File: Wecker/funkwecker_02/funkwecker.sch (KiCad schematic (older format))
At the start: 20 parts, among them J1 DCF77-Connector, J2 Debug-Interface, J3 LED-Display Connector (TM1637), SW1 Hauptschalter, U1 MCP1702-3302, U2 STM8L051F3P, U8 MCP1702-5002, Y1 HC49U 16MHz

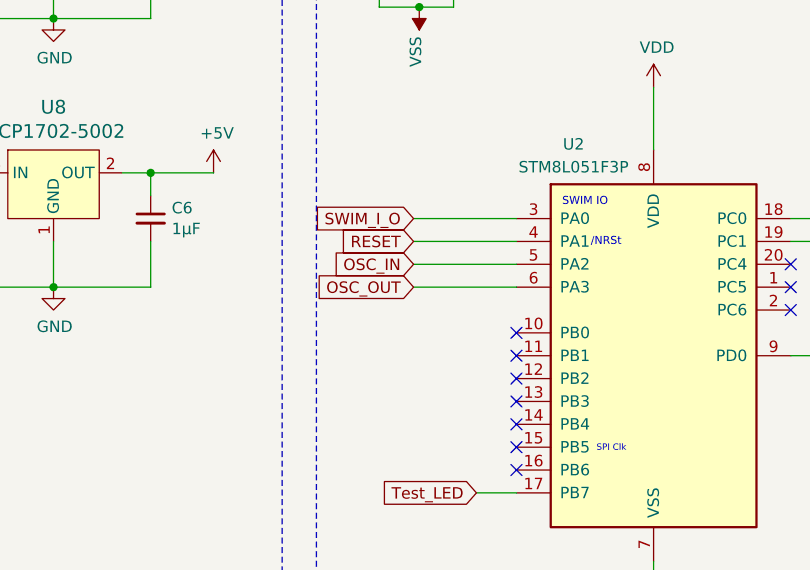
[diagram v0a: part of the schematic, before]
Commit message: 2.Revision angefangen
NRST Kondensator hinzugefügt
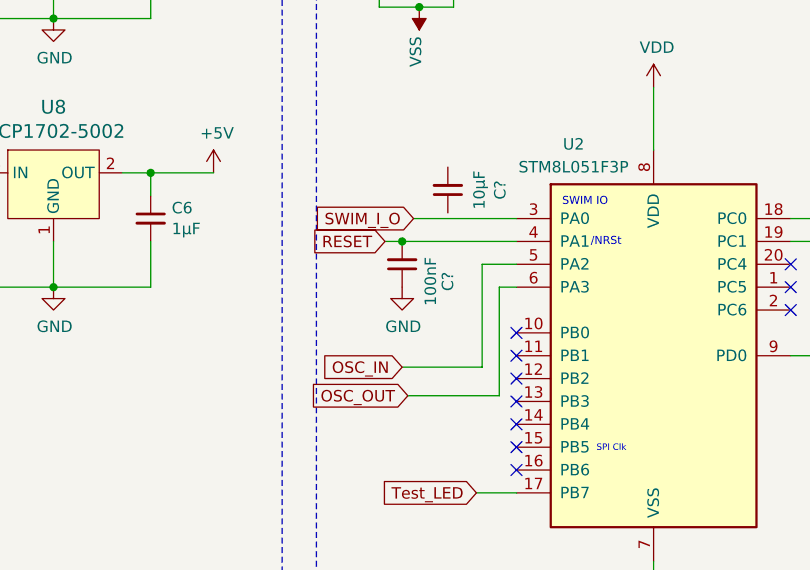
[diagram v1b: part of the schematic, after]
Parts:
- added C?: 10µF, Capacitor_THT:C_Disc_D7.0mm_W2.5mm_P5.00mm, symbol funkwecker-rescue:C_Small-Device
- added C?: 100nF, Capacitor_THT:C_Disc_D7.0mm_W2.5mm_P5.00mm, symbol funkwecker-rescue:C_Small-Device
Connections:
- net GND: now also C?.1
- net RESET: now also C?.2
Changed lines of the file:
@@
 Sheet 1 1
 Title "Funkwecker"
-Date "2021-12-12"
-Rev "0.1"
+Date "2021-12-21"
+Rev "0.2"
 Comp ""
 Comment1 ""
@@
 Text Notes 3075 800  0    50   ~ 0
 µC\n
-Text GLabel 3450 2675 0    50   Input ~ 0
+Text GLabel 3325 2675 0    50   Input ~ 0
 RESET
 Text GLabel 3450 2575 0    50   Input ~ 0
@@
 Text Notes 4250 3600 0    28   ~ 0
 SPI Clk\n
-Wire Wire Line
-	3900 2675 3450 2675
 Text GLabel 3725 3775 0    50   Input ~ 0
 Test_LED
 Wire Wire Line
 	3725 3775 3900 3775
-Text GLabel 3450 2875 0    50   Input ~ 0
+Text GLabel 3425 3350 0    50   Input ~ 0
 OSC_OUT
 $Comp
@@
 	1    0    0    -1
 $EndComp
-Text GLabel 3450 2775 0    50   Input ~ 0
+Text GLabel 3400 3225 0    50   Input ~ 0
 OSC_IN
-Wire Wire Line
-	3450 2775 3900 2775
-Wire Wire Line
-	3450 2875 3900 2875
 NoConn ~ 5100 2875
 NoConn ~ 5100 2975
@@
 	0    -1   -1   0
 $EndComp
+$Comp
+L funkwecker-rescue:C_Small-Device C?
+U 1 1 61C20B95
+P 3600 2450
+F 0 "C?" V 3371 2450 50  0000 C CNN
+F 1 "10µF" V 3462 2450 50  0000 C CNN
+F 2 "Capacitor_THT:C_Disc_D7.0mm_W2.5mm_P5.00mm" H 3600 2450 50  0001 C CNN
+F 3 "~" H 3600 2450 50  0001 C CNN
+	1    3600 2450
+	-1   0    0    1
+$EndComp
+$Comp
+L funkwecker-rescue:C_Small-Device C?
+U 1 1 61C265FF
+P 3400 2775
+F 0 "C?" V 3200 2850 50  0000 C CNN
+F 1 "100nF" V 3275 2850 50  0000 C CNN
+F 2 "Capacitor_THT:C_Disc_D7.0mm_W2.5mm_P5.00mm" H 3400 2775 50  0001 C CNN
+F 3 "~" H 3400 2775 50  0001 C CNN
+	1    3400 2775
+	-1   0    0    1
+$EndComp
+Wire Wire Line
+	3325 2675 3400 2675
+Connection ~ 3400 2675
+Wire Wire Line
+	3400 2675 3900 2675
+$Comp
+L funkwecker-rescue:GND-power #PWR?
+U 1 1 61C2841D
+P 3400 2875
+F 0 "#PWR?" H 3400 2625 50  0001 C CNN
+F 1 "GND" H 3405 2702 50  0000 C CNN
+F 2 "" H 3400 2875 50  0001 C CNN
+F 3 "" H 3400 2875 50  0001 C CNN
+	1    3400 2875
+	1    0    0    -1
+$EndComp
+Wire Wire Line
+	3900 2875 3825 2875
+Wire Wire Line
+	3825 2875 3825 3350
+Wire Wire Line
+	3825 3350 3425 3350
+Wire Wire Line
+	3900 2775 3750 2775
+Wire Wire Line
+	3750 2775 3750 3225
+Wire Wire Line
+	3750 3225 3400 3225
 $EndSCHEMATC

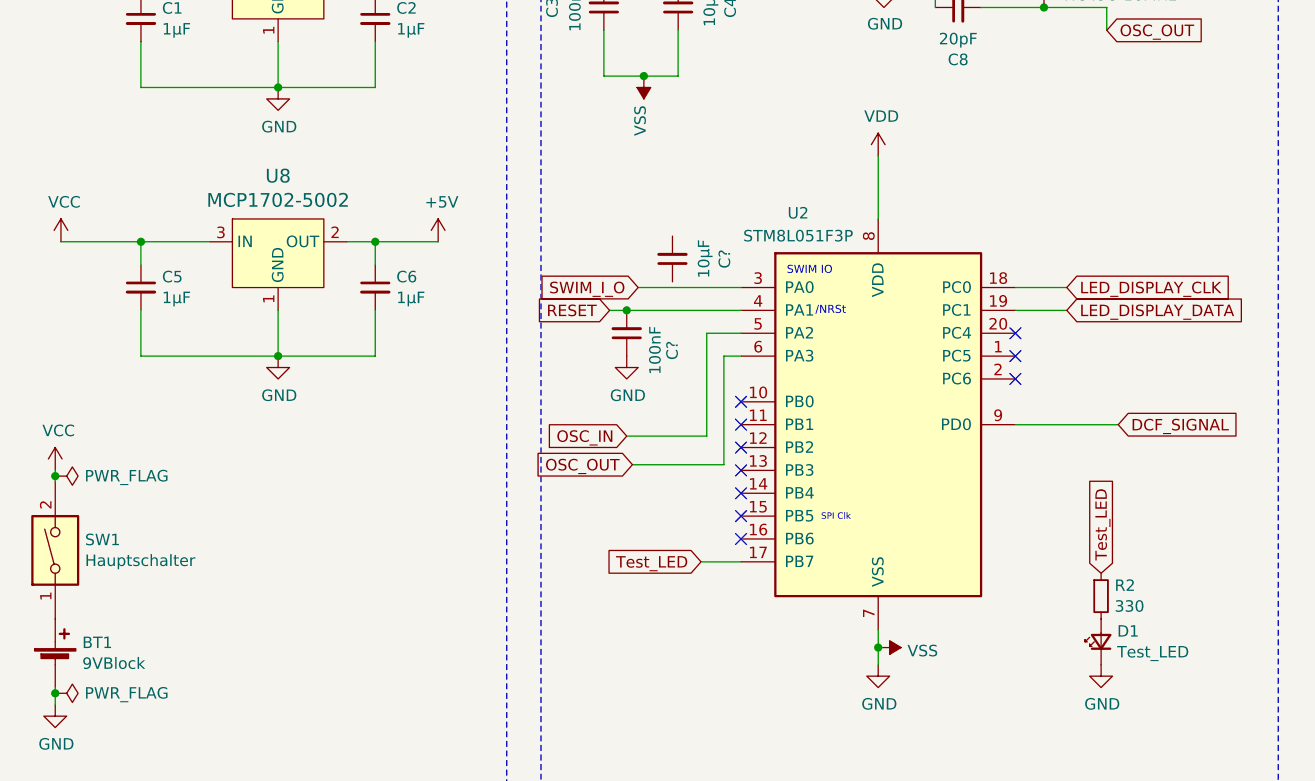
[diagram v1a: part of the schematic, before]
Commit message: Rev 2: Fehler korrigiert und neue Anordnung
Fehler:
-Fehlender Kondensator am RESET-Pin
-Fehlerhaftes Layout für beide Spannungsregler korrigiert
-Benötigten Platz verringert
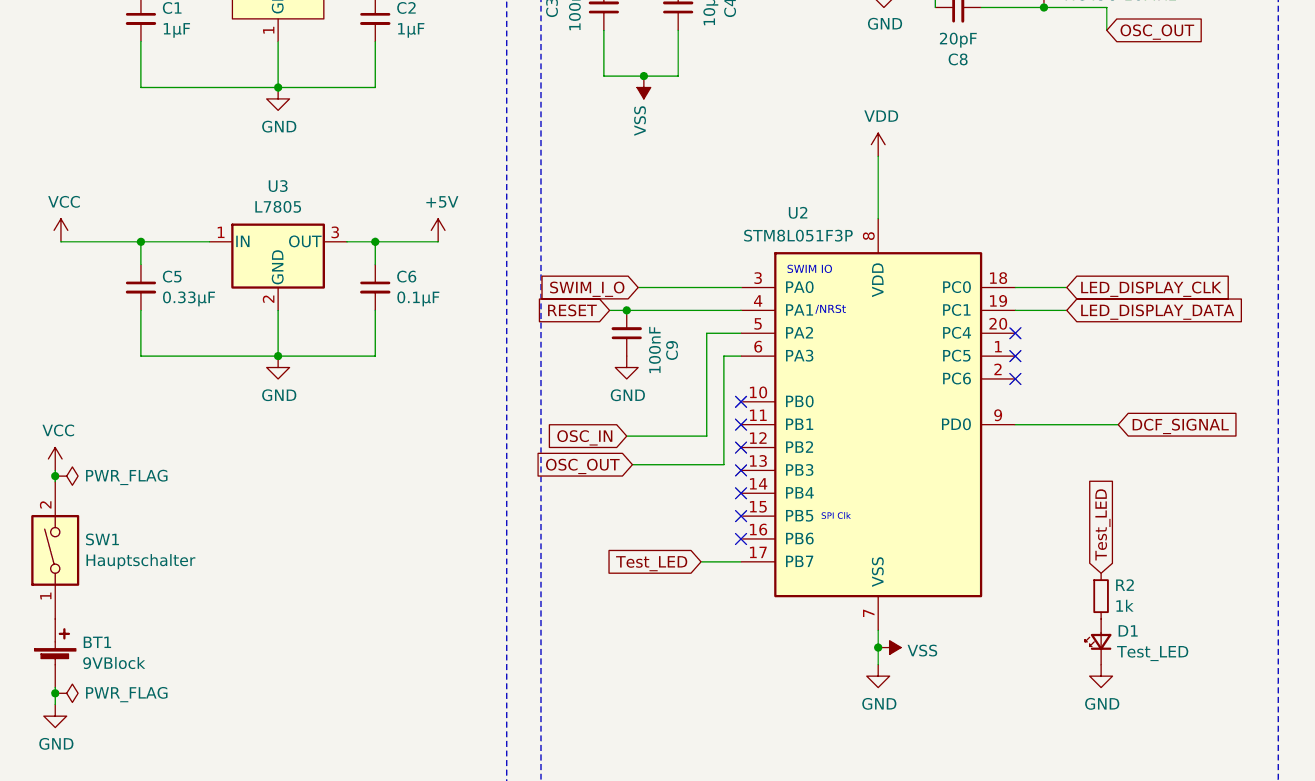
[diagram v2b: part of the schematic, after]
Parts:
- removed C?: 10µF, Capacitor_THT:C_Disc_D7.0mm_W2.5mm_P5.00mm, symbol funkwecker-rescue:C_Small-Device
- removed U8: MCP1702-5002, Package_TO_SOT_THT:TO-92, symbol funkwecker-rescue:MCP1700T-3302E_TT-dk_PMIC-Voltage-Regulators-Linear
- added U3: L7805, Package_TO_SOT_THT:TO-220-3_Vertical, symbol Regulator_Linear:L7805
- C1, C2: footprint Capacitor_THT:CP_Radial_D10.0mm_P2.50mm -> Capacitor_THT:C_Disc_D7.0mm_W2.5mm_P5.00mm
- C5: value 1µF -> 0.33µF; footprint Capacitor_THT:CP_Radial_D10.0mm_P2.50mm -> Capacitor_THT:C_Disc_D7.0mm_W2.5mm_P5.00mm
- C6: value 1µF -> 0.1µF; footprint Capacitor_THT:CP_Radial_D10.0mm_P2.50mm -> Capacitor_THT:C_Disc_D7.0mm_W2.5mm_P5.00mm
- R2: value 330 -> 1k
- gave numbers to parts that had none: 1
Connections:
- net +5V: now also U3.3 (OUT)
- net GND: now also U3.2 (GND)
- net VCC: now also U3.1 (IN)
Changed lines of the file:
@@
 F 0 "C1" H 1367 1446 50  0000 L CNN
 F 1 "1µF" H 1367 1355 50  0000 L CNN
-F 2 "Capacitor_THT:CP_Radial_D10.0mm_P2.50mm" H 1275 1400 50  0001 C CNN
+F 2 "Capacitor_THT:C_Disc_D7.0mm_W2.5mm_P5.00mm" H 1275 1400 50  0001 C CNN
 F 3 "~" H 1275 1400 50  0001 C CNN
 	1    1275 1400
@@
 F 0 "C2" H 2392 1446 50  0000 L CNN
 F 1 "1µF" H 2392 1355 50  0000 L CNN
-F 2 "Capacitor_THT:CP_Radial_D10.0mm_P2.50mm" H 2300 1400 50  0001 C CNN
+F 2 "Capacitor_THT:C_Disc_D7.0mm_W2.5mm_P5.00mm" H 2300 1400 50  0001 C CNN
 F 3 "~" H 2300 1400 50  0001 C CNN
 	1    2300 1400
@@
 	2300 1700 1875 1700
 $Comp
-L funkwecker-rescue:VCC-power #PWR0102
-U 1 1 61AA11C1
-P 925 1200
-F 0 "#PWR0102" H 925 1050 50  0001 C CNN
-F 1 "VCC" H 940 1373 50  0000 C CNN
-F 2 "" H 925 1200 50  0001 C CNN
-F 3 "" H 925 1200 50  0001 C CNN
-	1    925  1200
-	1    0    0    -1
-$EndComp
-$Comp
 L funkwecker-rescue:VCC-power #PWR0104
 U 1 1 61AA832C
@@
 F 3 "" H 900 3375 50  0001 C CNN
 	1    900  3375
-	1    0    0    -1
-$EndComp
-$Comp
-L funkwecker-rescue:VDD-power #PWR0105
-U 1 1 61AA994D
-P 2575 1200
-F 0 "#PWR0105" H 2575 1050 50  0001 C CNN
-F 1 "VDD" H 2590 1373 50  0000 C CNN
-F 2 "" H 2575 1200 50  0001 C CNN
-F 3 "" H 2575 1200 50  0001 C CNN
-	1    2575 1200
 	1    0    0    -1
 $EndComp
@@
 P 5475 3925
 F 0 "R2" H 5534 3971 50  0000 L CNN
-F 1 "330" H 5534 3880 50  0000 L CNN
+F 1 "1k" H 5534 3880 50  0000 L CNN
 F 2 "Resistor_THT:R_Axial_DIN0309_L9.0mm_D3.2mm_P12.70mm_Horizontal" H 5475 3925 50  0001 C CNN
 F 3 "~" H 5475 3925 50  0001 C CNN
@@
 	4500 4150 4500 4225
 $Comp
-L funkwecker-rescue:MCP1700T-3302E_TT-dk_PMIC-Voltage-Regulators-Linear U8
-U 1 1 61CCF659
-P 1875 2375
-F 0 "U8" H 1875 2662 60  0000 C CNN
-F 1 "MCP1702-5002" H 1875 2556 60  0000 C CNN
-F 2 "Package_TO_SOT_THT:TO-92" H 2075 2575 60  0001 L CNN
-F 3 "http://www.microchip.com/mymicrochip/filehandler.aspx?ddocname=en011779" H 2075 2675 60  0001 L CNN
-F 4 "MCP1700T3302ETTCT-ND" H 2075 2775 60  0001 L CNN "Digi-Key_PN"
-F 5 "MCP1700T-3302E/TT" H 2075 2875 60  0001 L CNN "MPN"
-F 6 "Integrated Circuits (ICs)" H 2075 2975 60  0001 L CNN "Category"
-F 7 "PMIC - Voltage Regulators - Linear" H 2075 3075 60  0001 L CNN "Family"
-F 8 "http://www.microchip.com/mymicrochip/filehandler.aspx?ddocname=en011779" H 2075 3175 60  0001 L CNN "DK_Datasheet_Link"
-F 9 "/product-detail/en/microchip-technology/MCP1700T-3302E-TT/MCP1700T3302ETTCT-ND/652677" H 2075 3275 60  0001 L CNN "DK_Detail_Page"
-F 10 "IC REG LINEAR 3.3V 250MA SOT23-3" H 2075 3375 60  0001 L CNN "Description"
-F 11 "Microchip Technology" H 2075 3475 60  0001 L CNN "Manufacturer"
-F 12 "Active" H 2075 3575 60  0001 L CNN "Status"
-	1    1875 2375
-	1    0    0    -1
-$EndComp
-$Comp
 L funkwecker-rescue:C_Small-Device C5
 U 1 1 61CCF65F
 P 1275 2575
 F 0 "C5" H 1367 2621 50  0000 L CNN
-F 1 "1µF" H 1367 2530 50  0000 L CNN
-F 2 "Capacitor_THT:CP_Radial_D10.0mm_P2.50mm" H 1275 2575 50  0001 C CNN
+F 1 "0.33µF" H 1367 2530 50  0000 L CNN
+F 2 "Capacitor_THT:C_Disc_D7.0mm_W2.5mm_P5.00mm" H 1275 2575 50  0001 C CNN
 F 3 "~" H 1275 2575 50  0001 C CNN
 	1    1275 2575
@@
 P 2300 2575
 F 0 "C6" H 2392 2621 50  0000 L CNN
-F 1 "1µF" H 2392 2530 50  0000 L CNN
-F 2 "Capacitor_THT:CP_Radial_D10.0mm_P2.50mm" H 2300 2575 50  0001 C CNN
+F 1 "0.1µF" H 2392 2530 50  0000 L CNN
+F 2 "Capacitor_THT:C_Disc_D7.0mm_W2.5mm_P5.00mm" H 2300 2575 50  0001 C CNN
 F 3 "~" H 2300 2575 50  0001 C CNN
 	1    2300 2575
@@
 $EndComp
 $Comp
-L funkwecker-rescue:C_Small-Device C?
-U 1 1 61C20B95
-P 3600 2450
-F 0 "C?" V 3371 2450 50  0000 C CNN
-F 1 "10µF" V 3462 2450 50  0000 C CNN
-F 2 "Capacitor_THT:C_Disc_D7.0mm_W2.5mm_P5.00mm" H 3600 2450 50  0001 C CNN
-F 3 "~" H 3600 2450 50  0001 C CNN
-	1    3600 2450
-	-1   0    0    1
-$EndComp
-$Comp
-L funkwecker-rescue:C_Small-Device C?
+L funkwecker-rescue:C_Small-Device C9
 U 1 1 61C265FF
 P 3400 2775
-F 0 "C?" V 3200 2850 50  0000 C CNN
+F 0 "C9" V 3200 2850 50  0000 C CNN
 F 1 "100nF" V 3275 2850 50  0000 C CNN
 F 2 "Capacitor_THT:C_Disc_D7.0mm_W2.5mm_P5.00mm" H 3400 2775 50  0001 C CNN
@@
 	3400 2675 3900 2675
 $Comp
-L funkwecker-rescue:GND-power #PWR?
+L funkwecker-rescue:GND-power #PWR0116
 U 1 1 61C2841D
 P 3400 2875
-F 0 "#PWR?" H 3400 2625 50  0001 C CNN
+F 0 "#PWR0116" H 3400 2625 50  0001 C CNN
 F 1 "GND" H 3405 2702 50  0000 C CNN
 F 2 "" H 3400 2875 50  0001 C CNN
@@
 Wire Wire Line
 	3750 3225 3400 3225
+$Comp
+L funkwecker-rescue:VDD-power #PWR0105
+U 1 1 61AA994D
+P 2575 1200
+F 0 "#PWR0105" H 2575 1050 50  0001 C CNN
+F 1 "VDD" H 2590 1373 50  0000 C CNN
+F 2 "" H 2575 1200 50  0001 C CNN
+F 3 "" H 2575 1200 50  0001 C CNN
+	1    2575 1200
+	1    0    0    -1
+$EndComp
+$Comp
+L funkwecker-rescue:VCC-power #PWR0102
+U 1 1 61AA11C1
+P 925 1200
+F 0 "#PWR0102" H 925 1050 50  0001 C CNN
+F 1 "VCC" H 940 1373 50  0000 C CNN
+F 2 "" H 925 1200 50  0001 C CNN
+F 3 "" H 925 1200 50  0001 C CNN
+	1    925  1200
+	1    0    0    -1
+$EndComp
+$Comp
+L Regulator_Linear:L7805 U3
+U 1 1 61C84B96
+P 1875 2375
+F 0 "U3" H 1875 2617 50  0000 C CNN
+F 1 "L7805" H 1875 2526 50  0000 C CNN
+F 2 "Package_TO_SOT_THT:TO-220-3_Vertical" H 1900 2225 50  0001 L CIN
+F 3 "http://www.st.com/content/ccc/resource/technical/document/datasheet/41/4f/b3/b0/12/d4/47/88/CD00000444.pdf/files/CD00000444.pdf/jcr:content/translations/en.CD00000444.pdf" H 1875 2325 50  0001 C CNN
+	1    1875 2375
+	1    0    0    -1
+$EndComp
 $EndSCHEMATC
